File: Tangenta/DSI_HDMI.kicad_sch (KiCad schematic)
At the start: 47 parts, among them J8 HDMI_19PIN_043, Q3 2N7002, Q4 2N7002, U13 LT8912B

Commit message: SMbus done right...
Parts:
- removed Q3, Q4: 2N7002, NMOS_2N7002:NMOS_2N7002, symbol NMOS_2N7002:2N7002
- removed R2 (x2): 1.8k, Resistor_SMD:R_0402_1005Metric, symbol Device:R_Small_US
- added Q3, Q4: BSS138, Package_TO_SOT_SMD:SOT-23, symbol Transistor_FET:BSS138
- R2: value 2k -> 1.8k
- R2: value 1.8k -> 4.7k
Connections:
- net 1V8: now also Q3.1 (G), Q4.1 (G)
- net I2C_2_DSI.SCL: now also Q4.2 (S)
- net I2C_2_DSI.SDA: now also Q3.2 (S)
- net I2C_HDMI_SCL: now also Q4.3 (D)
- net I2C_HDMI_SDA: now also Q3.3 (D)

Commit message: Libraries exported from global to project.
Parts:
- C1: symbol Device:C_Small -> CholaSymbolsPrjLib:C_Small
- D2: symbol B540C-13-F:B540C-13-F -> CholaSymbolsPrjLib:B540C-13-F
- FB1: symbol Ferrite_Bead_100:GZ2012D101TF -> CholaSymbolsPrjLib:GZ2012D101TF
- J8: symbol HDMI_CONNECTOR:HDMI_19PIN_043 -> CholaSymbolsPrjLib:HDMI_19PIN_043
- OSC1: symbol 25MHZ_OSCILLATOR:OT322525MJBA4SL -> CholaSymbolsPrjLib:OT322525MJBA4SL
- Q3, Q4: symbol Transistor_FET:BSS138 -> CholaSymbolsPrjLib:BSS138
- R2: symbol Device:R_Small_US -> CholaSymbolsPrjLib:R_Small_US
- U13: symbol LT8912B:LT8912B -> CholaSymbolsPrjLib:LT8912B

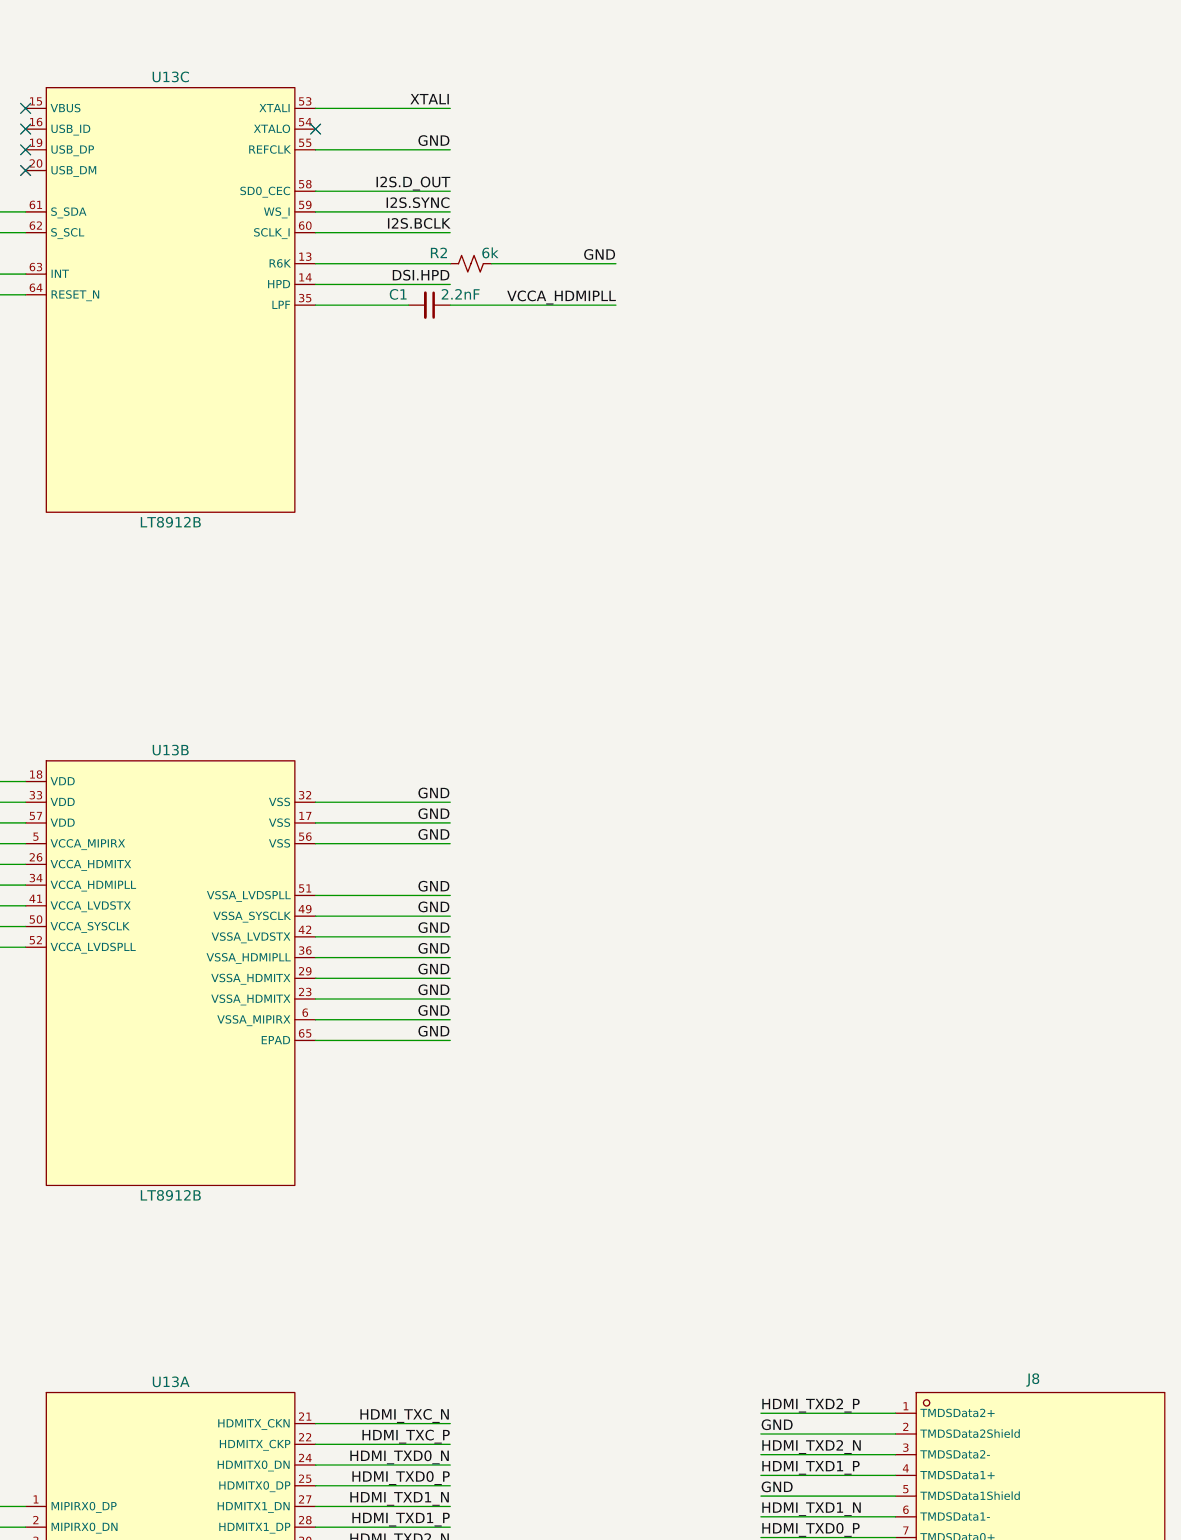
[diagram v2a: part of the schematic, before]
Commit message: Re-annotated. Ready for JLCPCB design verification.
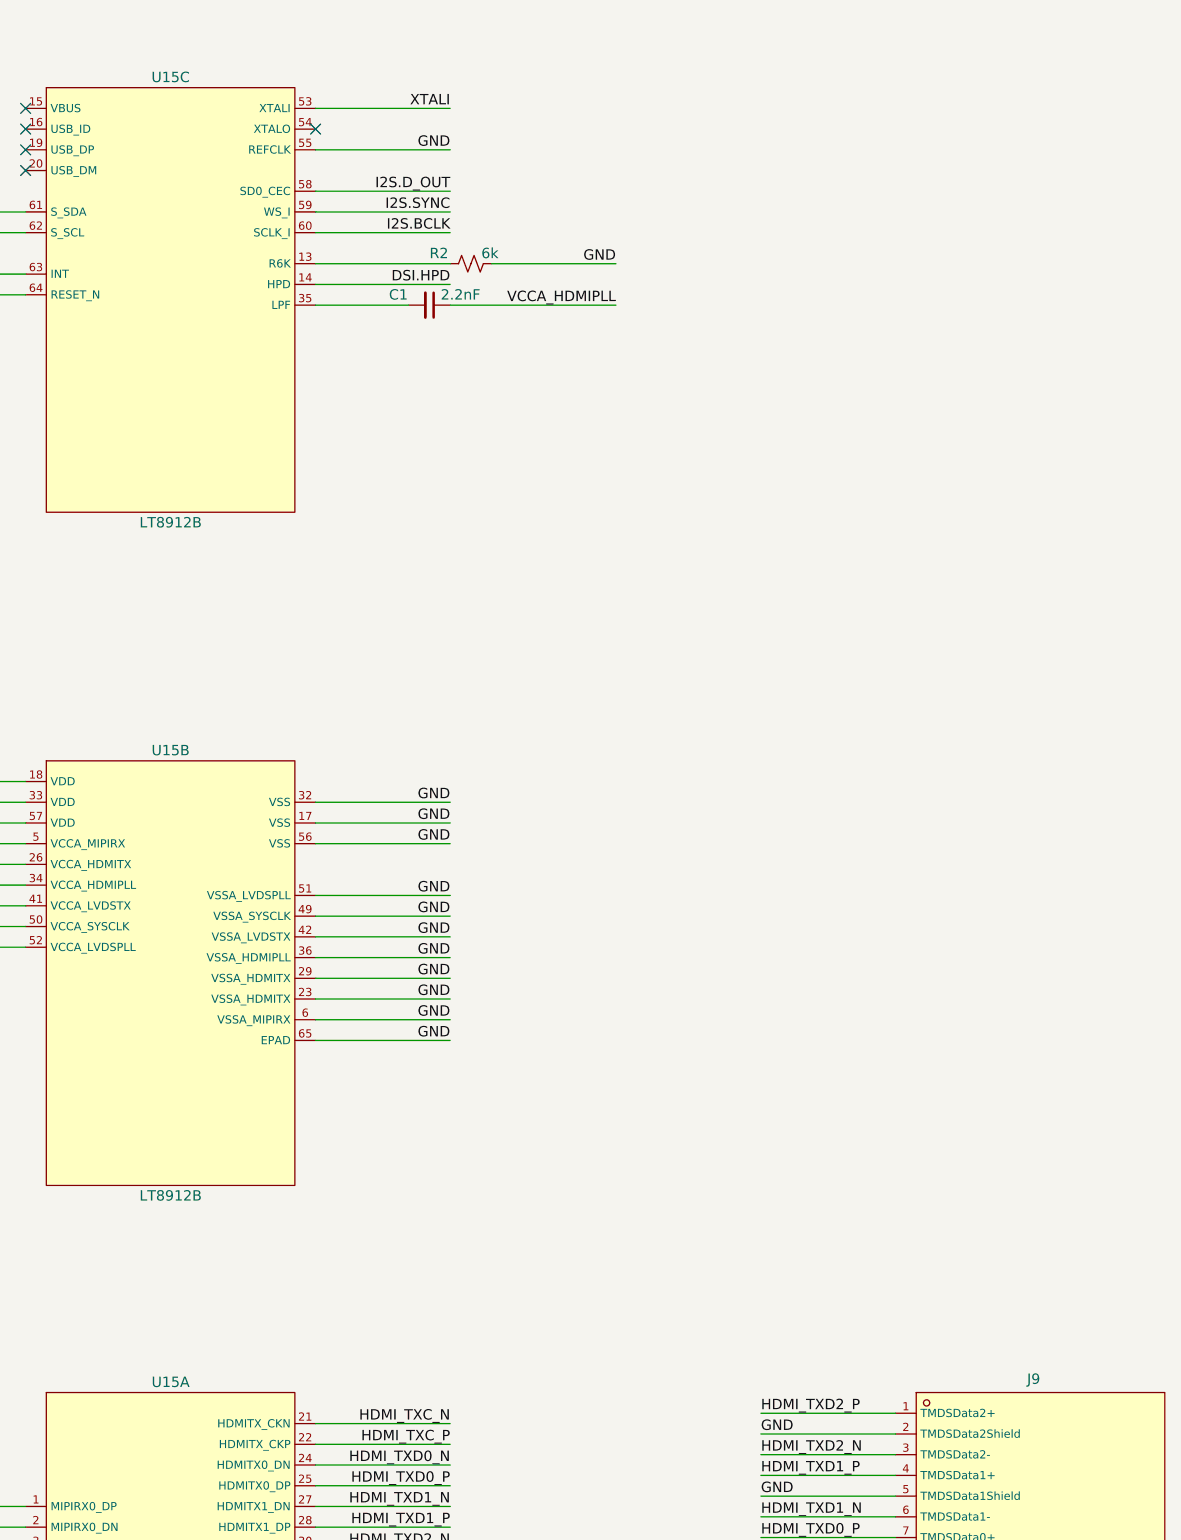
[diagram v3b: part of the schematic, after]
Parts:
- renumbered J8 to J9, U13 to U15

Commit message: ...
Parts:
- C1: symbol CholaSymbolsPrjLib:C_Small -> LocalPrjLib:C_Small
- D2: symbol CholaSymbolsPrjLib:B540C-13-F -> LocalPrjLib:B540C-13-F
- FB1: symbol CholaSymbolsPrjLib:GZ2012D101TF -> LocalPrjLib:GZ2012D101TF
- J9: symbol CholaSymbolsPrjLib:HDMI_19PIN_043 -> LocalPrjLib:HDMI_19PIN_043
- OSC1: symbol CholaSymbolsPrjLib:OT322525MJBA4SL -> LocalPrjLib:OT322525MJBA4SL
- Q3, Q4: symbol CholaSymbolsPrjLib:BSS138 -> LocalPrjLib:BSS138
- R2: symbol CholaSymbolsPrjLib:R_Small_US -> LocalPrjLib:R_Small_US
- U15: symbol CholaSymbolsPrjLib:LT8912B -> LocalPrjLib:LT8912B

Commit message: Fixes, new approach.
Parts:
- C1: symbol LocalPrjLib:C_Small -> LocalSymbolsPrjLib:C_Small
- D2: symbol LocalPrjLib:B540C-13-F -> LocalSymbolsPrjLib:B540C-13-F
- FB1: symbol LocalPrjLib:GZ2012D101TF -> LocalSymbolsPrjLib:GZ2012D101TF
- J9: symbol LocalPrjLib:HDMI_19PIN_043 -> LocalSymbolsPrjLib:HDMI_19PIN_043
- OSC1: symbol LocalPrjLib:OT322525MJBA4SL -> LocalSymbolsPrjLib:OT322525MJBA4SL
- Q3, Q4: symbol LocalPrjLib:BSS138 -> LocalSymbolsPrjLib:BSS138
- R2: symbol LocalPrjLib:R_Small_US -> LocalSymbolsPrjLib:R_Small_US
- U15: symbol LocalPrjLib:LT8912B -> LocalSymbolsPrjLib:LT8912B

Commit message: Fixes...
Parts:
- renumbered C1 to C73, C1 to C74, C1 to C75, C1 to C76, C1 to C77, C1 to C78, C1 to C79, C1 to C80, C1 to C81, C1 to C82, C1 to C83, C1 to C84, C1 to C85, C1 to C86, C1 to C87, C1 to C88, C1 to C89, C1 to C90, C1 to C91, C1 to C92, C1 to C93, C1 to C94, C1 to C95, C1 to C96, C1 to C97, D2 to D6, FB1 to FB2, FB1 to FB3, FB1 to FB4, FB1 to FB5, FB1 to FB6, FB1 to FB7, FB1 to FB8, FB1 to FB9, R2 to R47, R2 to R48, R2 to R49, R2 to R50, R2 to R51, R2 to R52
